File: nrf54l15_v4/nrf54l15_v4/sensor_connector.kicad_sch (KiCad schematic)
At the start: 1 part, among them CN1 SM04B-SRSS-TB

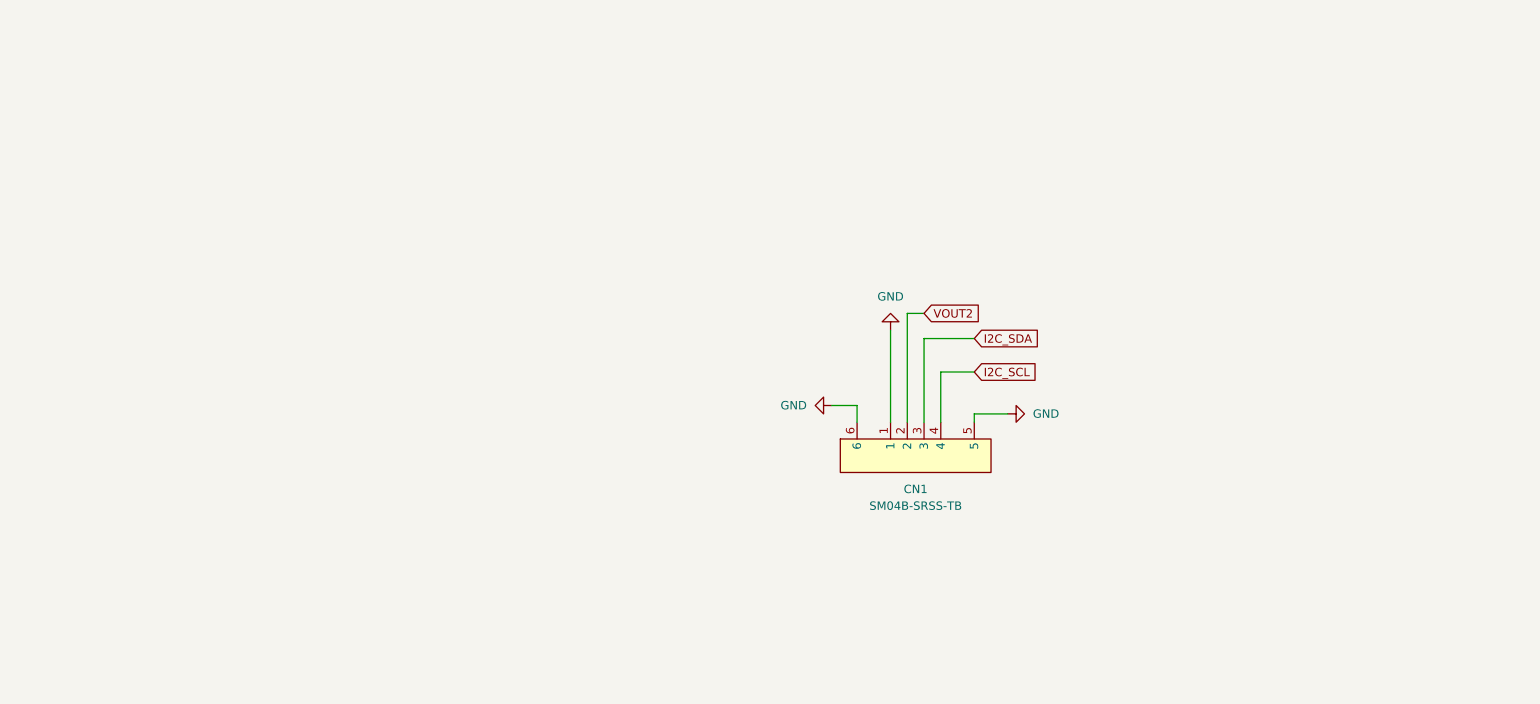
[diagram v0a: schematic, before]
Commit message: Update nrf54l15_v4 design; add feather board, enclosure, and docs
nrf54l15_v4:
- Sensor connector (CN1) reworked to a 14-pin Molex 503480-1400 FFC
  connector with a project footprint library (nrf54l15_v4.pretty) and
  vendor drawing/3D model.
- nRF54L15 pin assignment fixes for the sensor bus (I2C, SPI/UART, INT,
  AIN, board-ID).
- AEM10330 solar block: EN_SLEEP tied to GND, MPPT ratio set to 70%,
  MPNs added to C40-C43.
- Annotation cleanup across antenna, npm1300 and power_supply sheets;
  PCB updated from schematic; zone min clearance set to 0.5 mm.
- Add 3D-printable enclosure generator and STL outputs.

New:
- nrf54l15_feather KiCad project.
- Sensor_Boards/Conductivity_Salinity design notes.
- solar-analysis-v4.md and v4-sensor-connector.md design docs.
- AEM10330 and PowerFilm LL200-2.4-75 datasheets.

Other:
- nrf54l15_v2 BOM: fix misplaced capacitance value columns (C9/C11);
  add .xlsx BOM.
- .gitignore: ignore dated schematic backups, extra claude_bak copies,
  vendor zip downloads and DRC report exports.

Co-Authored-By: Claude Opus 5.5 <noreply@anthropic.com>
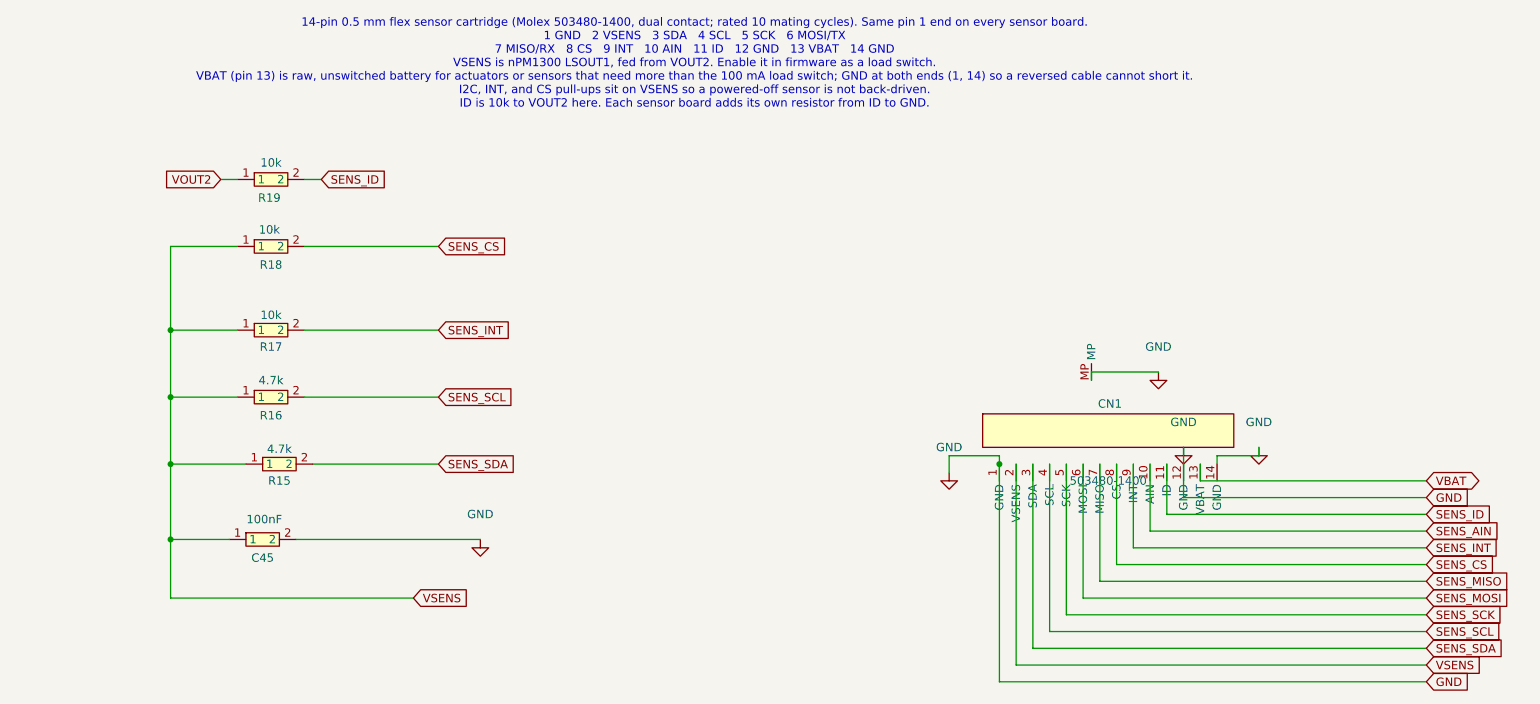
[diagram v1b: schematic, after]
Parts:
- removed CN1: SM04B-SRSS-TB, easyeda2kicad:CONN-SMD_4P-P1.00_SM04B-SRSS-TB-LF-SN, symbol EasyEDA2Kicad:SM04B-SRSS-TB
- added C45: 100nF, easyeda2kicad:C0402, symbol Device:C_0402
- added CN1: 503480-1400, nrf54l15_v4:Molex_503480-1400_1x14-1MP_P0.50mm_Horizontal, symbol Connector_FFC-FPC:Molex_503480-1400
- added R15, R16: 4.7k, easyeda2kicad:R0402, symbol Device:R_0402
- added R17, R18, R19: 10k, easyeda2kicad:R0402, symbol Device:R_0402
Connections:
- net GND: now also C45.2, CN1.1 (GND), CN1.12 (GND), CN1.14 (GND), CN1.MP
- net VOUT2: now also R19.1
- new net SENS_AIN: CN1.10 (AIN)
- new net SENS_CS: CN1.8 (CS), R18.2
- new net SENS_ID: CN1.11 (ID), R19.2
- new net SENS_INT: CN1.9 (INT), R17.2
- new net SENS_MISO: CN1.7 (MISO)
- new net SENS_MOSI: CN1.6 (MOSI)
- new net SENS_SCK: CN1.5 (SCK)
- new net SENS_SCL: CN1.4 (SCL), R16.2
- new net SENS_SDA: CN1.3 (SDA), R15.2
- new net VBAT: CN1.13 (VBAT)
- new net VSENS: C45.1, CN1.2 (VSENS), R15.1, R16.1, R17.1, R18.1
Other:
- note added: "14-pin 0.5 mm flex sensor cartridge (Molex 503480-1400, dual contact; rated 10 mating cycles). Same pin 1 end on every sensor board. 1 GND 2 VSENS 3 SDA 4 SCL 5 SCK 6 MOSI/TX 7 MISO/RX 8 CS 9 INT 10 AIN 11 ID 12 GND 13 VBAT 14 GND VSENS is nPM1300 LSOUT1, fed from VOUT2. Enable it in firmware as a load switch. VBAT (pin 13) is raw, unswitched battery for actuators or sensors that need more than t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"
